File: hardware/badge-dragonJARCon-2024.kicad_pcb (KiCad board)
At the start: 2 copper layers, 97.9 x 100 mm, 38 parts, among them J1 UART, J2 Battery, J3 OLED, J5 Shitty addon, P1 USB_C_Plug_USB2.0, Q1 DMG3415U-7, SW1 ON, SW2 RESET, SW3 BOOT, SW4 PB4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

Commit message: feat(Hw): Start new floorplan
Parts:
- removed J2: Battery, Footprints:BAT-TH_BH-AAA-A1AJ024
- removed the Ref** at (130.4, 81.4)
- added BH1: BAT-TH_BH-AAA-A1AJ024, Footprints:BAT-TH_BH-AAA-A1AJ024, B.Cu at (157.5, 64.8)
- added Ref**: Val**, Footprints:Badge_DragonJAR_2024_Serigrafia, F.Cu at (216.1, 77.5)
- C1, C2, D1, J1, P1, Q1, R1, SW1, U1, U2: moved to B.Cu
- moved F1 216.3 mm to (47.1, 62.6)
- moved C10 205.4 mm to (37.1, 55.9)
- moved C11 205.4 mm to (37.1, 58.4)
- moved C3 205.4 mm to (33.1, 55.9)
- moved C4 205.4 mm to (33.1, 58.4)
- moved C9 205.4 mm to (37.1, 53.4)
- moved R2 205.4 mm to (37.1, 63.4)
- moved R3 205.4 mm to (37.1, 66.0)
- moved R4 205.4 mm to (41.1, 50.9)
- moved R5 205.4 mm to (41.1, 53.4)
- moved R7 205.4 mm to (41.1, 55.9)
- moved R8 205.4 mm to (41.1, 58.4)
- moved SW2 144.9 mm to (68.0, 58.4)
- moved SW3 144.9 mm to (68.0, 65.5)
- moved U1 115.4 mm to (194.5, 46.3), turned to 150 degrees
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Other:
- board size 97.9 x 100 mm -> 104.7 x 107 mm

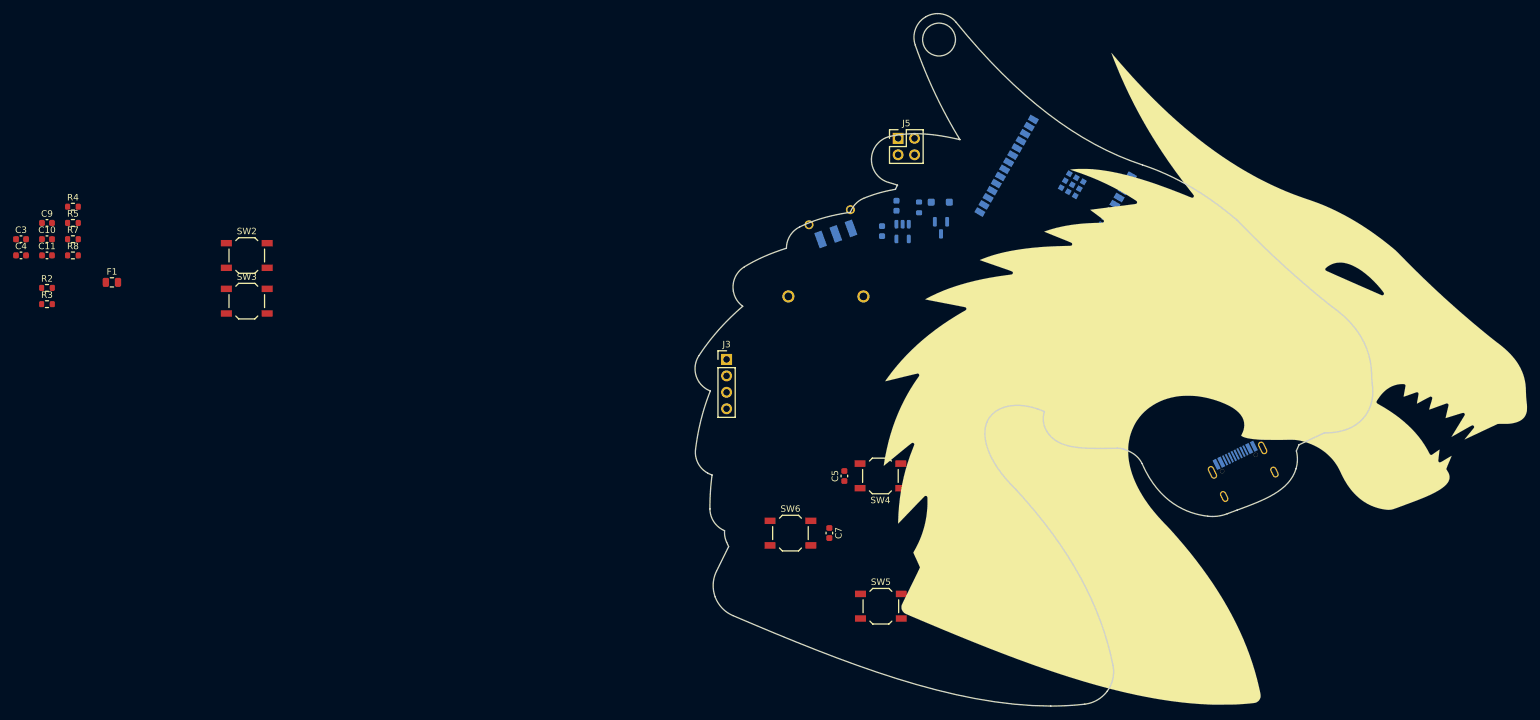
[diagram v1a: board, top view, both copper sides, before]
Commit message: feat(Hw): Init routing
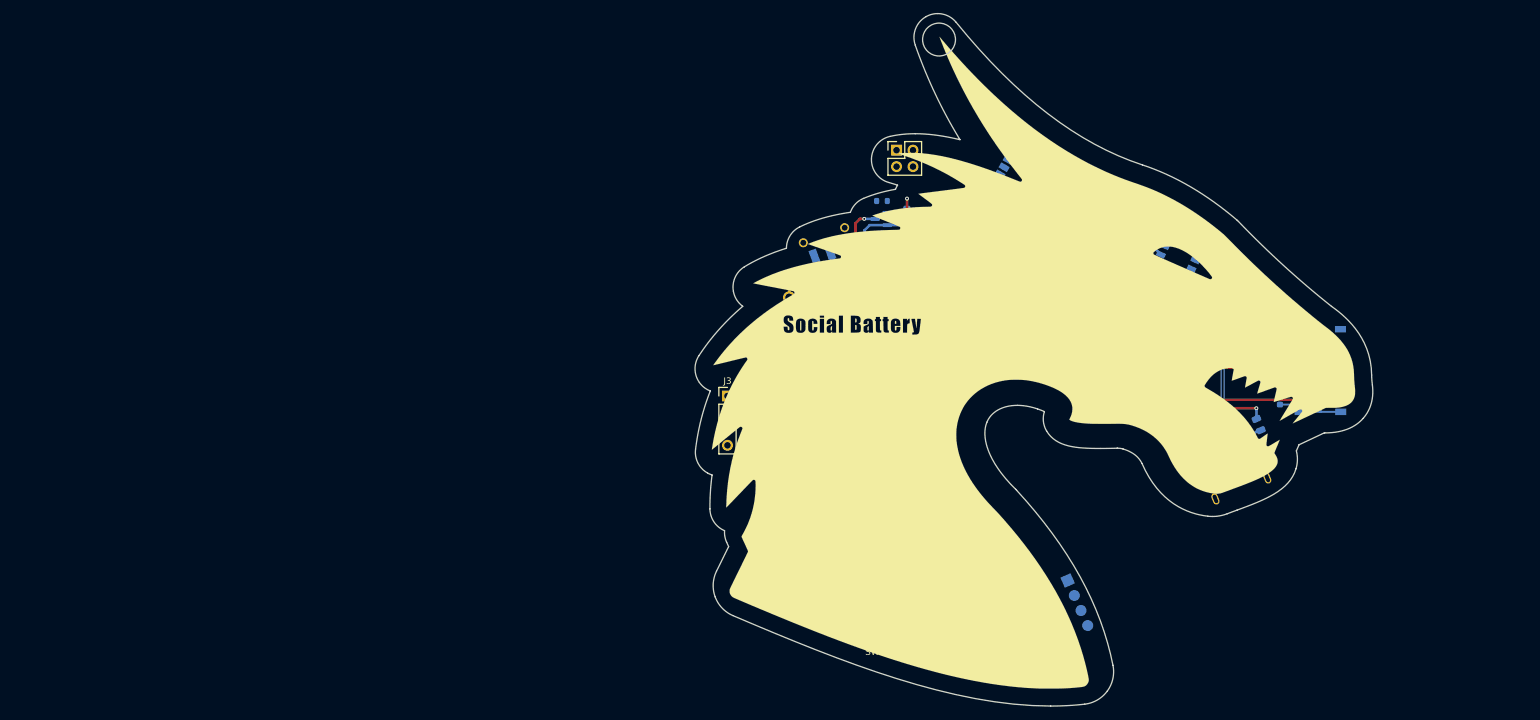
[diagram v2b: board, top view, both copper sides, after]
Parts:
- removed BH1: BAT-TH_BH-AAA-A1AJ024, Footprints:BAT-TH_BH-AAA-A1AJ024
- removed the Ref** at (216.1, 77.5)
- added D10: Orange, LED_SMD:LED_0805_2012Metric, F.Cu at (157.0, 73.6)
- added D3: Green, LED_SMD:LED_0805_2012Metric, F.Cu at (169.0, 73.6)
- added D4: Red, LED_SMD:LED_0805_2012Metric, F.Cu at (154.0, 73.6)
- added D5: Yellow, LED_SMD:LED_0805_2012Metric, F.Cu at (163.0, 73.6)
- added D6: Yellow, LED_SMD:LED_0805_2012Metric, F.Cu at (166.0, 73.6)
- added D7: Red, LED_SMD:LED_0805_2012Metric, F.Cu at (151.0, 73.6)
- added D8: Green, LED_SMD:LED_0805_2012Metric, F.Cu at (172.0, 73.6)
- added D9: Orange, LED_SMD:LED_0805_2012Metric, F.Cu at (160.0, 73.6)
- added J2: Battery, Footprints:BAT-TH_BH-AAA-A1AJ024, B.Cu at (157.6, 64.9)
- added R6: 3.3K, Resistor_SMD:R_0603_1608Metric, B.Cu at (199.1, 62.1)
- added RN1: R_Pack04, Resistor_SMD:R_Array_Convex_4x0603, F.Cu at (167.3, 82.0)
- added RN2: R_Pack04, Resistor_SMD:R_Array_Convex_4x0603, F.Cu at (155.4, 82.0)
- added Ref**: Val**, Footprints:Badge_DragonJAR_2024_cuerpo, F.Cu at (189.5, 75.0)
- C10, C11, C3, C4, C9, F1, R2, R3, R4, R5, R7, R8, SW2, SW3: moved to B.Cu
- J1: footprint Connector_PinHeader_2.54mm:PinHeader_1x05_P2.54mm_Vertical -> Footprints:PinHeader_1x04_P2.54mm_Vertical
- moved C3 196.1 mm to (227.6, 80.7), turned to -90 degrees
- moved C4 194.8 mm to (227.4, 71.2)
- moved R4 187.6 mm to (227.4, 72.7), turned to 180 degrees
- moved R2 185.2 mm to (220.9, 86.5), turned to -158 degrees
- moved R3 180.6 mm to (216.4, 88.2), turned to 22 degrees
- moved R8 179.1 mm to (220.2, 60.1), turned to 155 degrees
- moved R7 178.6 mm to (219.6, 61.4), turned to 155 degrees
- moved F1 178.6 mm to (224.3, 84.6), turned to 112 degrees
- moved R5 178.1 mm to (219.0, 62.8), turned to 155 degrees
- moved C9 169.1 mm to (206.2, 54.6), turned to 60 degrees
- moved C10 167.8 mm to (204.9, 53.9), turned to 60 degrees
- moved C11 166.6 mm to (203.6, 53.2), turned to 60 degrees
- moved SW3 166.6 mm to (233.9, 80.7), turned to 180 degrees
- moved SW2 166.4 mm to (233.8, 71.7), turned to 180 degrees
- moved Ref** 29.0 mm to (212.6, 59.3)
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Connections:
- U1 pad 10: unconnected-(U1-IO8-Pad10) -> /IO8
- U1 pad 16: unconnected-(U1-IO18-Pad16) -> /BG2
- U1 pad 17: unconnected-(U1-IO19-Pad17) -> /BY1
- U1 pad 18: unconnected-(U1-IO20-Pad18) -> /BY2
- U1 pad 19: unconnected-(U1-IO21-Pad19) -> /BO1
- U1 pad 20: /BACK -> /BO2
- U1 pad 21: /DOWN -> /BR1
- U1 pad 23: /UP -> /BR2
- U1 pad 4: unconnected-(U1-IO4-Pad4) -> /BG1
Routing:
- net /BOOT: track 0.00 -> 89.0 mm, vias 0 -> 2
- net VBUS: track 0.00 -> 88.5 mm, vias 0 -> 2
- net /EN: track 0.00 -> 66.0 mm, vias 0 -> 2
- net /D+: track 0.00 -> 52.8 mm
- net /D-: track 0.00 -> 52.4 mm
- net +BATT: track 0.00 -> 23.8 mm, vias 0 -> 1
- net Net-(SW1-B): track 0.00 -> 15.8 mm
- net +3V3: track 0.00 -> 12.8 mm
- net Net-(F1-Pad1): track 0.00 -> 12.7 mm
- net Net-(D2-BK): track 0.00 -> 12.1 mm
- net Net-(D1-K): track 0.00 -> 11.8 mm
- net /GPIO22: track 0.00 -> 9.74 mm
- net /GPIO15: track 0.00 -> 9.62 mm
- net Net-(D8-K): track 0.00 -> 9.54 mm
- net Net-(D9-K): track 0.00 -> 9.44 mm
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
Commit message: feat(Hw): Update PCB
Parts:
- added kibuzzard-664257DB: G***, kibuzzard-664257DB, F.Cu at (166.4, 42.2)
- added kibuzzard-6642586D: G***, kibuzzard-6642586D, F.Cu at (166.4, 44.7)
- added kibuzzard-664258CC: G***, kibuzzard-664258CC, B.Cu at (193.6, 110.5)
- added kibuzzard-664258F1: G***, kibuzzard-664258F1, B.Cu at (193.1, 113.1)
- added kibuzzard-6642590C: G***, kibuzzard-6642590C, B.Cu at (193.1, 115.6)
- added kibuzzard-66425921: G***, kibuzzard-66425921, B.Cu at (193.3, 118.2)
- added kibuzzard-66425A11: G***, kibuzzard-66425A11, B.Cu at (234.0, 76.4)
- added kibuzzard-66425A5E: G***, kibuzzard-66425A5E, B.Cu at (233.8, 67.4)
- moved J1 5.14 mm to (190.0, 110.5), turned to 180 degrees
- moved J5 0.73 mm to (169.1, 42.2)
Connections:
- C5 pad 2: /GPIO1 -> /UP
- C6 pad 2: /GPIO22 -> /DOWN
- C7 pad 2: /GPIO15 -> /BACK
- C8 pad 2: /GPIO23 -> /SELECT
- J1 pad 2: /RX -> /TX
- J1 pad 3: /TX -> /RX
- J3 pad 1: +3V3 -> /SDA
- J3 pad 2: GND -> /SCL
- J3 pad 3: /SCL -> +3V3
- J3 pad 4: /SDA -> GND
- J5 pad 2: /SCL -> /SDA
- J5 pad 4: /SDA -> /SCL
- RN1 pad 3: Net-(D5-K) -> Net-(D6-K)
- RN1 pad 4: Net-(D6-K) -> Net-(D5-K)
- SW4 pad 2: /GPIO1 -> /UP
- SW5 pad 2: /GPIO22 -> /DOWN
- SW6 pad 2: /GPIO15 -> /BACK
- SW7 pad 2: /GPIO23 -> /SELECT
- U1 pad 11: unconnected-(U1-IO10-Pad11) -> /SELECT
- U1 pad 12: /BLUE -> /RED
- U1 pad 26: /GREEN -> /BLUE
- U1 pad 27: /RED -> /GREEN
- U1 pad 5: unconnected-(U1-IO5-Pad5) -> /BACK
- U1 pad 8: unconnected-(U1-IO0-Pad8) -> /UP
- U1 pad 9: /SELECT -> /DOWN
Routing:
- net +3V3: track 12.8 -> 236.4 mm, vias 0 -> 8
- net /SDA: track 0.00 -> 113.4 mm, vias 0 -> 1
- net /SCL: track 0.00 -> 111.8 mm, vias 0 -> 3
- net /BACK: track 0.00 -> 100.7 mm, vias 0 -> 1
- net /RX: track 0.00 -> 96.2 mm, vias 0 -> 2
- net /TX: track 0.00 -> 93.8 mm, vias 0 -> 2
- net /DOWN: track 0.00 -> 91.4 mm, vias 0 -> 1
- net /UP: track 0.00 -> 73.2 mm, vias 0 -> 1
- net /SELECT: track 0.00 -> 62.7 mm, vias 0 -> 1
- net /BR2: track 0.00 -> 55.0 mm, vias 0 -> 1
- net /GREEN: track 0.00 -> 52.2 mm
- net /BR1: track 0.00 -> 48.5 mm, vias 0 -> 1
- net /BLUE: track 0.00 -> 47.8 mm
- net /BO2: track 0.00 -> 43.8 mm, vias 0 -> 1
- net /BG1: track 0.00 -> 43.2 mm, vias 0 -> 1
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- added copper zone on B.Cu, net GND
- added copper zone on F.Cu, net GND

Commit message: feat(hw): add logos
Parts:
- added G***: LOGO, LOGO, B.Cu at (215.0, 74.4)
- added G***: LOGO, Aesthetics:electronic_cats_logo_8x6, B.Cu at (197.8, 73.0)

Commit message: feat(hw): add links
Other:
- board text added: "Badge DragonJarCON"
- board text added: "v1.0"

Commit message: feat(): add more labels
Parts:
- added G***: LOGO, Aesthetics:pcbway_13x4, B.Cu at (207.3, 85.9)
- added Ref**: Val**, Aesthetics:heart, F.Cu at (204.3, 68.2)
- added kibuzzard-66450F45: G***, kibuzzard-66450F45, B.Cu at (179.2, 41.6)
- added kibuzzard-664510CB: G***, kibuzzard-664510CB, B.Cu at (163.5, 54.6)
- added kibuzzard-664510D9: G***, kibuzzard-664510D9, B.Cu at (151.6, 58.9)
- moved G*** 4.46 mm to (193.8, 71.2)
- moved G*** 2.36 mm to (217.4, 74.2)
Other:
- board text added: "El Dragon rojo ha despertado, no te sientas seguro en ningun lado, lee con cuidado, porque su ojo te esta hablando"
- board text added: "Hecho con"
- board text added: "La mejor defensa es un buen ataque."
- board text added: "Mexico"
- board text added: "Parcero usted termina enguayabado"
- board text added: "github.com/ElectronicCats/badge-dragonJARCon-2024"

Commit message: feat(Hw): Labels moved
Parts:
- moved G*** 0.53 mm to (193.8, 70.6)

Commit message: feat(Hw): Update BOM
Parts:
- F1: value 0.5A -> 0.75A; footprint Fuse:Fuse_0805_2012Metric -> Fuse:Fuse_0603_1608Metric
- SW1: footprint Footprints:JS102011SAQN -> Footprints:MSK12C02
- moved SW1 1.99 mm to (157.0, 55.1)
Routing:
- net Net-(SW1-B): track 15.8 -> 14.2 mm
